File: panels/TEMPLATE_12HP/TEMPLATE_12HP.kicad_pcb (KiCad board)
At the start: 2 copper layers, 60.1 x 128.4 mm, 5 parts

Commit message: cleanup; added ext board
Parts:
- added REF**: Panel_LCD-015M002B, IMNOTWOPR:Panel_LCD-015M002B, F.Cu at (96.8, 99.2)
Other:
- board size 60.1 x 128.4 mm -> 60.6 x 128.4 mm

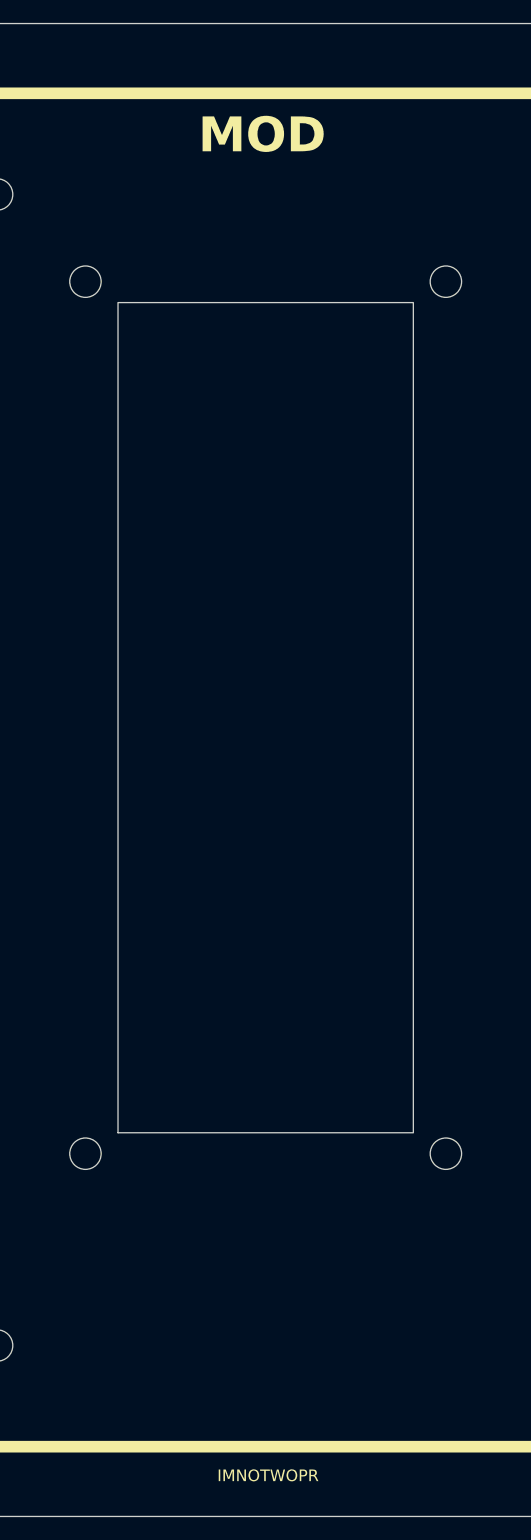
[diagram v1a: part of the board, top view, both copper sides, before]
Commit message: mega updates.  psg module.  ferrous & example makefiles overhaul
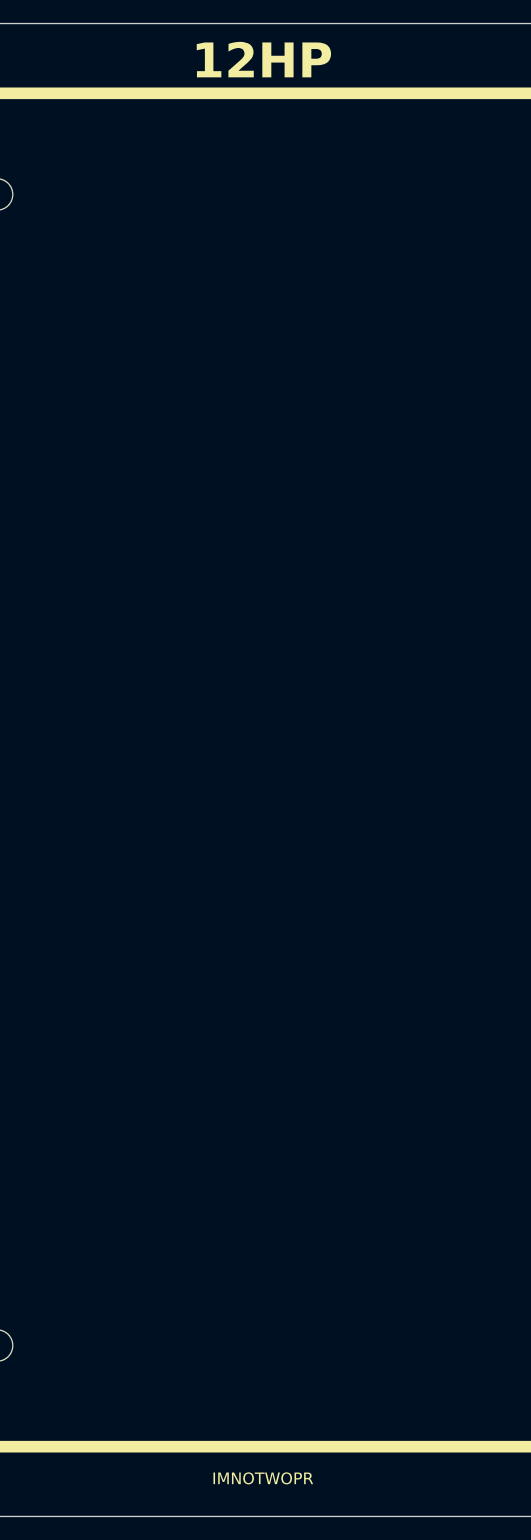
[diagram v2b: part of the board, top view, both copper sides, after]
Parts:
- removed the REF** at (96.8, 99.2)
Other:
- board text added: "${TITLE}"
- board text removed: "MOD"
